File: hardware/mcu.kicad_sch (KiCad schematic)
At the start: 0 parts

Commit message: Add MCU sheet
ESP32-S3-WROOM-1-N8 with 3V3 decoupling, EN RC with reset button,
GPIO0 pull-up with boot button, eject button, status LED, USB series
resistors with DNP filter caps, UART and SPI clock series resistors,
and Tag-Connect TC2030-NL service footprint (excluded from BOM).
Module pin assignment per docs/PCB_DESIGN.md.

Co-Authored-By: Claude Opus 5.5 <noreply@anthropic.com>
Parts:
- added C301: 100uF, Capacitor_SMD:C_1210_3225Metric, symbol Device:C
- added C302: 10uF, Capacitor_SMD:C_0805_2012Metric, symbol Device:C
- added C303: 100nF, Capacitor_SMD:C_0402_1005Metric, symbol Device:C
- added C304: 1uF, Capacitor_SMD:C_0402_1005Metric, symbol Device:C
- added C305, C306, C307, C308: DNP, Capacitor_SMD:C_0402_1005Metric, symbol Device:C
- added D301: Green, LED_SMD:LED_0603_1608Metric, symbol Device:LED
- added J301: TC2030-NL, Connector:Tag-Connect_TC2030-IDC-NL_2x03_P1.27mm_Vertical, symbol Connector_Generic:Conn_02x03_Odd_Even
- added R301, R302: 10k, Resistor_SMD:R_0402_1005Metric, symbol Device:R
- added R303: 1k, Resistor_SMD:R_0402_1005Metric, symbol Device:R
- added R304, R305, R309, R310: 0R, Resistor_SMD:R_0402_1005Metric, symbol Device:R
- added R306: 499R, Resistor_SMD:R_0402_1005Metric, symbol Device:R
- added R307, R308: 100R, Resistor_SMD:R_0402_1005Metric, symbol Device:R
- added SW301: RESET, symbol Switch:SW_Push
- added SW302: BOOT, symbol Switch:SW_Push
- added SW303: EJECT, symbol Switch:SW_Push
- added U301: ESP32-S3-WROOM-1-N8, RF_Module:ESP32-S3-WROOM-1, symbol RF_Module:ESP32-S3-WROOM-1
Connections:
- new net +3V3: C301.1, C302.1, C303.1, J301.1 (Pin_1), R301.1, R302.1, U301.2 (3V3)
- new net BOOT: J301.5 (Pin_5), R302.2, SW302.1, U301.27 (IO0)
- new net EJECT: SW303.1, U301.4 (IO4)
- new net EN: C304.1, J301.3 (Pin_3), R301.2, SW301.1, U301.3 (EN)
- new net GND: C301.2, C302.2, C303.2, C304.2, C305.2, C306.2, C307.2, C308.2, D301.1 (K), J301.6 (Pin_6), SW301.2, SW302.2, SW303.2, U301.1 (GND), U301.40 (GND), U301.41 (GND)
- new net GNSS_PPS: U301.24 (IO47)
- new net GNSS_RESET_N: U301.7 (IO7)
- new net GNSS_RXD: R307.2
- new net GNSS_TXD: R308.2
- new net IO12_SCK: R309.1, U301.20 (IO12)
- new net IO16_SCK: R310.1, U301.9 (IO16)
- new net IO17_TX: R307.1, U301.10 (IO17)
- new net IO18_RX: R308.1, U301.11 (IO18)
- new net IO19_DN: C306.1, R305.2, U301.13 (USB_D-)
- new net IO20_DP: C305.1, R304.2, U301.14 (USB_D+)
- new net LED: R303.1, U301.38 (IO2)
- new net LED_A: D301.2 (A), R303.2
- new net LORA_DIO0: U301.25 (IO48)
- new net LORA_DIO1: U301.35 (IO42)
- new net LORA_MISO: U301.23 (IO21)
- new net LORA_MOSI: U301.8 (IO15)
- new net LORA_NSS: U301.22 (IO14)
- new net LORA_RESET: U301.31 (IO38)
- new net LORA_SCK: C308.1, R310.2
- new net OLED_RES: U301.34 (IO41)
- new net OLED_SCL: U301.17 (IO9)
- new net OLED_SDA: U301.12 (IO8)
- new net SD_CS: U301.18 (IO10)
- new net SD_MISO: U301.21 (IO13)
- new net SD_MOSI: U301.19 (IO11)
- new net SD_SCK: C307.1, R309.2
- new net TXD0_R: R306.1, U301.37 (TXD0)
- new net UART0_RX: J301.4 (Pin_4), U301.36 (RXD0)
- new net UART0_TX: J301.2 (Pin_2), R306.2
- new net USB_DN: R305.1
- new net USB_DP: R304.1
- new net VBUS_SENSE: U301.5 (IO5)
- no-connect marks 0 -> 10

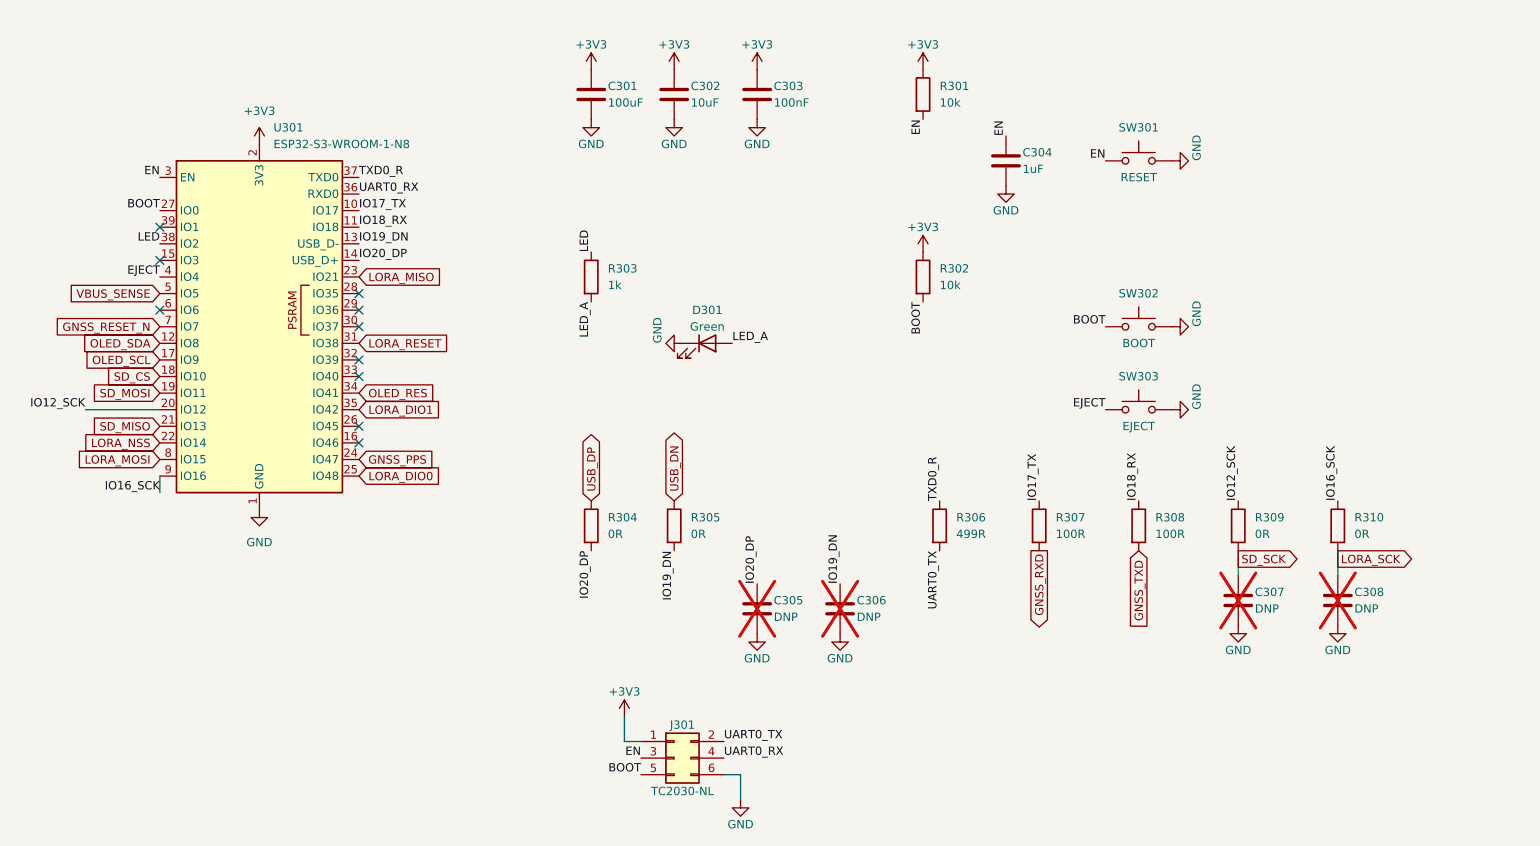
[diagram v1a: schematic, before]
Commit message: Complete schematic, place and partially route the PCB
Schematic:
- Add Storage & Display sheet (microSD, FH12 OLED connector, TLV75801
  3.8 V VBAT regulator, charge-pump parts) and Radio sheet fixes
- Select remaining parts (PTS810, 1206L075THYR, SMF5.0A, MCP120 EN
  supervisor DNP, Elna DSK backup cap), add mounting holes and fiducials
- Pin changes for routability: PPS -> IO15, LoRa MOSI -> IO47,
  LoRa RESET -> IO48, LoRa DIO0 -> IO1
- Remove optional SPI clock filter parts (R309/C307, R310/C308)
- Remove company name from title blocks (personal project)

PCB (60 x 120 mm, 4 layers):
- Place all parts; GNSS zone with custom DRC rules (kicad_dru)
- Project ESP32-S3-WROOM-1 footprint with 0.4 mm thermal vias
- GND / +3V3 / +5V copper zones
- Route power path, GNSS, microSD and LoRa buses
- DRC clean except unrouted nets and expected silkscreen-at-edge items

Docs: selected-parts table, pin table and EMC deviation in PCB_DESIGN.md

Co-Authored-By: Claude Opus 5.5 <noreply@anthropic.com>
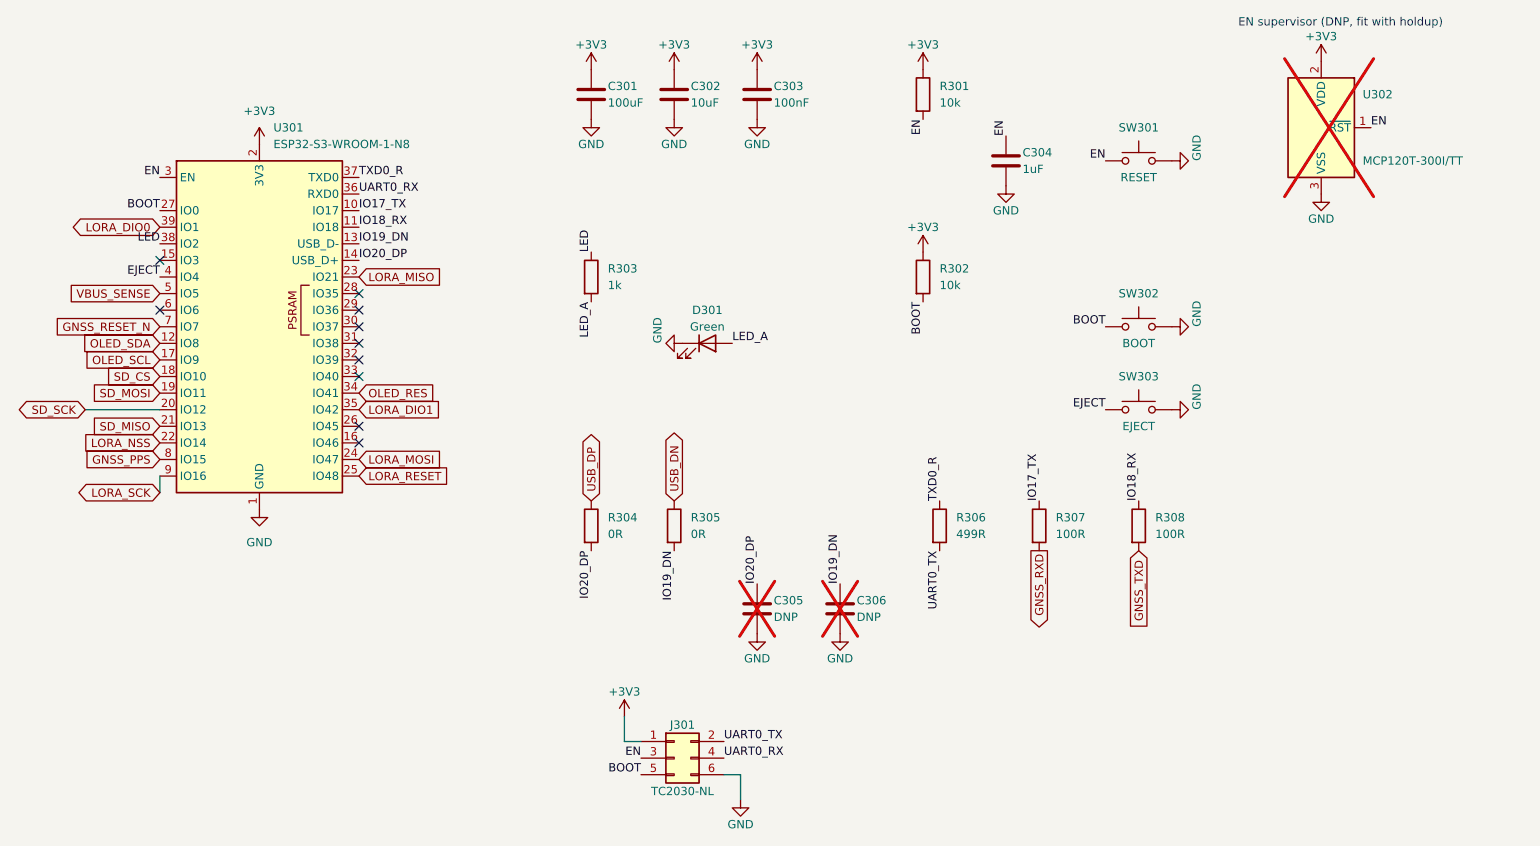
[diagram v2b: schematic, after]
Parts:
- removed C307, C308: DNP, Capacitor_SMD:C_0402_1005Metric, symbol Device:C
- removed R309, R310: 0R, Resistor_SMD:R_0402_1005Metric, symbol Device:R
- added U302: MCP120T-300I/TT, Package_TO_SOT_SMD:SOT-23, symbol Power_Supervisor:MCP120-xxxxTT
- SW301, SW302, SW303: footprint (none) -> Button_Switch_SMD:SW_SPST_PTS810
- U301: footprint RF_Module:ESP32-S3-WROOM-1 -> gps-lora:ESP32-S3-WROOM-1
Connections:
- net IO12_SCK is gone; now on net SD_SCK: U301.20 (IO12)
- net IO16_SCK is gone; now on net LORA_SCK: U301.9 (IO16)
- net +3V3: now also U302.2 (VDD)
- net EN: now also U302.1 (~{RST})
- net GND: now also U302.3 (VSS)
- net GNSS_PPS: now also U301.8 (IO15); no longer U301.24 (IO47)
- net LORA_DIO0: now also U301.39 (IO1); no longer U301.25 (IO48)
- net LORA_MOSI: now also U301.24 (IO47); no longer U301.8 (IO15)
- net LORA_RESET: now also U301.25 (IO48); no longer U301.31 (IO38)
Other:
- note added: "EN supervisor (DNP, fit with holdup)"
- company: SSS-Defence -> (none)

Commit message: Finish PCB routing, add BOM part numbers and fab export
Routing (DRC: 0 errors, 0 unconnected; ERC: 0)
- Complete the remaining nets on top of the GUI routing; GND stitching
  grid and edge fence; every GND pad reaches the L2 plane
- Re-lay the microSD bus under USB D+ so the USBLC6 and VBUS TVS get
  direct GND vias; lift LoRa NSS/MISO/MOSI to clear the TVS via
- Reroute D-, VBUS sense, CC2, BOOT, OLED SDA/SCL, LED and TXD0_R; remove
  vias in pads (R205, R505, R204, R507, U301 pin 7)
- Placement tweaks: C306 moved, C508/C509/R508 rotated 180, R302 moved
- PCB title block with rev v0.1

Parts and outputs
- MPN and Manufacturer fields on all placed parts (tools/add-mpn.py)
- tools/fab-export.py: ERC/DRC gate, zone refill, Gerbers, drill, BOM,
  pick-and-place and fab notes for Lion Circuits
- OLED panel DS501: schematic symbol and board-only 3D footprint
- Elna DSK footprint for C403 (not placed yet)
- kicad-routing skill under .claude/skills

Open before fab (see docs/PCB_DESIGN.md Open items): J502 pin order is
mirrored against the panel FPC; Lion stackup widths; C403 placement.

Co-Authored-By: Claude Opus 5.5 <noreply@anthropic.com>
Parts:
- C301: MPN (none) -> GRM32ER61A107ME20L; Manufacturer (none) -> Murata
- C302: MPN (none) -> CL21A106KAYNNNE; Manufacturer (none) -> Samsung
- C303: MPN (none) -> CL05B104KO5NNNC; Manufacturer (none) -> Samsung
- C304: MPN (none) -> CL05A105KA5NQNC; Manufacturer (none) -> Samsung
- D301: MPN (none) -> LTST-C191KGKT; Manufacturer (none) -> Lite-On
- R301, R302: MPN (none) -> RC0402FR-0710KL; Manufacturer (none) -> Yageo
- R303: MPN (none) -> RC0402FR-071KL; Manufacturer (none) -> Yageo
- R304, R305: MPN (none) -> RC0402JR-070RL; Manufacturer (none) -> Yageo
- R306: MPN (none) -> RC0402FR-07499RL; Manufacturer (none) -> Yageo
- R307, R308: MPN (none) -> RC0402FR-07100RL; Manufacturer (none) -> Yageo
- SW301, SW302, SW303: MPN (none) -> PTS810 SJM 250 SMTR LFS; Manufacturer (none) -> C&K
- U301: MPN (none) -> ESP32-S3-WROOM-1-N8; Manufacturer (none) -> Espressif
- U302: MPN (none) -> MCP120T-300I/TT; Manufacturer (none) -> Microchip

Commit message: Rename project to Theoros and add V1.0 silkscreen artwork
Theoros (Greek θεωρός): an official observer and envoy, sent to watch
and report back.

Rename gps-lora to theoros everywhere: KiCad project, symbol and
footprint libraries, firmware library (theoros-core), umbrella header,
PC tool (tools/theoros.py), NVS namespaces, mDNS hostname, docs and
title blocks. The HKDF salt is now "theoros" (7 bytes), so every derived
key changes; the SECURITY.md test vectors are recomputed and host tests
pass. Boards provisioned with the old salt need re-provisioning.

Board revision is now V1.0. Silkscreen additions:
- Top: "THEOROS ${REVISION}" and "ΘΕΩΡΟΣ", an antenna warning next to
  J401, and a hidden line under the OLED panel.
- Bottom: an owl made as a solder-mask opening over the GND pour (gold
  with ENIG; vias inside stay tented) and the motto "ΟΡΩ ΚΑΙ ΑΓΓΕΛΛΩ /
  I SEE AND I REPORT".
Fab notes now state silkscreen on both sides and the intentional mask
opening. DRC is unchanged from before (4 silk-edge warnings).

Co-Authored-By: Claude Opus 5.5 <noreply@anthropic.com>
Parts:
- U301: footprint gps-lora:ESP32-S3-WROOM-1 -> theoros:ESP32-S3-WROOM-1
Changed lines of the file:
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@@
 		(title "MCU")
 		(date "2026-10-05")
-		(rev "v0.1")
+		(rev "V1.0")
 		(comment 1 "CERN-OHL-P-2.0")
-		(comment 2 "https://github.com/Majorwhiskey/gps-lora")
+		(comment 2 "https://github.com/Majorwhiskey/theoros")
 	)
 	(text "EN supervisor (DNP, fit with holdup)"
@@
 		)
 		(instances
-			(project "gps-lora"
+			(project "theoros"
 				(path "/4fe56230-194d-489d-a2bc-70162e8e6b48/4a1b2dd0-e07f-4468-b434-479773685126"
 					(reference "SW303")
@@
 		)
 		(instances
-			(project "gps-lora"
+			(project "theoros"
 				(path "/4fe56230-194d-489d-a2bc-70162e8e6b48/4a1b2dd0-e07f-4468-b434-479773685126"
 					(reference "R305")
@@
 		)
 		(instances
-			(project "gps-lora"
+			(project "theoros"
 				(path "/4fe56230-194d-489d-a2bc-70162e8e6b48/4a1b2dd0-e07f-4468-b434-479773685126"
 					(reference "SW301")
@@
 		)
 		(instances
-			(project "gps-lora"
+			(project "theoros"
 				(path "/4fe56230-194d-489d-a2bc-70162e8e6b48/4a1b2dd0-e07f-4468-b434-479773685126"
 					(reference "#PWR41")
@@
 		)
 		(instances
-			(project "gps-lora"
+			(project "theoros"
 				(path "/4fe56230-194d-489d-a2bc-70162e8e6b48/4a1b2dd0-e07f-4468-b434-479773685126"
 					(reference "C305")
@@
 		)
 		(instances
-			(project "gps-lora"
+			(project "theoros"
 				(path "/4fe56230-194d-489d-a2bc-70162e8e6b48/4a1b2dd0-e07f-4468-b434-479773685126"
 					(reference "#PWR35")
@@
 		)
 		(instances
-			(project "gps-lora"
+			(project "theoros"
 				(path "/4fe56230-194d-489d-a2bc-70162e8e6b48/4a1b2dd0-e07f-4468-b434-479773685126"
 					(reference "#PWR32")
@@
 		)
 		(instances
-			(project "gps-lora"
+			(project "theoros"
 				(path "/4fe56230-194d-489d-a2bc-70162e8e6b48/4a1b2dd0-e07f-4468-b434-479773685126"
 					(reference "C301")
@@
 		)
 		(instances
-			(project "gps-lora"
+			(project "theoros"
 				(path "/4fe56230-194d-489d-a2bc-70162e8e6b48/4a1b2dd0-e07f-4468-b434-479773685126"
 					(reference "R303")
@@
 			)
 		)
-		(property "Footprint" "gps-lora:ESP32-S3-WROOM-1"
+		(property "Footprint" "theoros:ESP32-S3-WROOM-1"
 			(at 88.9 114.3 0)
 			(hide yes)
@@
 		)
 		(instances
-			(project "gps-lora"
+			(project "theoros"
 				(path "/4fe56230-194d-489d-a2bc-70162e8e6b48/4a1b2dd0-e07f-4468-b434-479773685126"
 					(reference "#PWR028")
@@
 		)
 		(instances
-			(project "gps-lora"
+			(project "theoros"
 				(path "/4fe56230-194d-489d-a2bc-70162e8e6b48/4a1b2dd0-e07f-4468-b434-479773685126"
 					(reference "#PWR36")
@@
 		)
 		(instances
-			(project "gps-lora"
+			(project "theoros"
 				(path "/4fe56230-194d-489d-a2bc-70162e8e6b48/4a1b2dd0-e07f-4468-b434-479773685126"
 					(reference "#PWR39")
@@
 		)
 		(instances
-			(project "gps-lora"
+			(project "theoros"
 				(path "/4fe56230-194d-489d-a2bc-70162e8e6b48/4a1b2dd0-e07f-4468-b434-479773685126"
 					(reference "#PWR601")
@@
 		)
 		(instances
-			(project "gps-lora"
+			(project "theoros"
 				(path "/4fe56230-194d-489d-a2bc-70162e8e6b48/4a1b2dd0-e07f-4468-b434-479773685126"
 					(reference "SW302")
@@
 		)
 		(instances
-			(project "gps-lora"
+			(project "theoros"
 				(path "/4fe56230-194d-489d-a2bc-70162e8e6b48/4a1b2dd0-e07f-4468-b434-479773685126"
 					(reference "#PWR602")
@@
 			)
 		)
-		(property "Footprint" "gps-lora:ESP32-S3-WROOM-1"
+		(property "Footprint" "theoros:ESP32-S3-WROOM-1"
 			(at 88.9 83.82 0)
 			(hide yes)
@@
 		)
 		(instances
-			(project "gps-lora"
+			(project "theoros"
 				(path "/4fe56230-194d-489d-a2bc-70162e8e6b48/4a1b2dd0-e07f-4468-b434-479773685126"
 					(reference "U301")
@@
 		)
 		(instances
-			(project "gps-lora"
+			(project "theoros"
 				(path "/4fe56230-194d-489d-a2bc-70162e8e6b48/4a1b2dd0-e07f-4468-b434-479773685126"
 					(reference "#PWR50")
@@
 		)
 		(instances
-			(project "gps-lora"
+			(project "theoros"
 				(path "/4fe56230-194d-489d-a2bc-70162e8e6b48/4a1b2dd0-e07f-4468-b434-479773685126"
 					(reference "#PWR33")
@@
 		)
 		(instances
-			(project "gps-lora"
+			(project "theoros"
 				(path "/4fe56230-194d-489d-a2bc-70162e8e6b48/4a1b2dd0-e07f-4468-b434-479773685126"
 					(reference "R308")
@@
 		)
 		(instances
-			(project "gps-lora"
+			(project "theoros"
 				(path "/4fe56230-194d-489d-a2bc-70162e8e6b48/4a1b2dd0-e07f-4468-b434-479773685126"
 					(reference "C303")
@@
 		)
 		(instances
-			(project "gps-lora"
+			(project "theoros"
 				(path "/4fe56230-194d-489d-a2bc-70162e8e6b48/4a1b2dd0-e07f-4468-b434-479773685126"
 					(reference "#PWR38")
@@
 		)
 		(instances
-			(project "gps-lora"
+			(project "theoros"
 				(path "/4fe56230-194d-489d-a2bc-70162e8e6b48/4a1b2dd0-e07f-4468-b434-479773685126"
 					(reference "U302")
@@
 		)
 		(instances
-			(project "gps-lora"
+			(project "theoros"
 				(path "/4fe56230-194d-489d-a2bc-70162e8e6b48/4a1b2dd0-e07f-4468-b434-479773685126"
 					(reference "R304")
@@
 		)
 		(instances
-			(project "gps-lora"
+			(project "theoros"
 				(path "/4fe56230-194d-489d-a2bc-70162e8e6b48/4a1b2dd0-e07f-4468-b434-479773685126"
 					(reference "R301")
@@
 		)
 		(instances
-			(project "gps-lora"
+			(project "theoros"
 				(path "/4fe56230-194d-489d-a2bc-70162e8e6b48/4a1b2dd0-e07f-4468-b434-479773685126"
 					(reference "#PWR37")
@@
 		)
 		(instances
-			(project "gps-lora"
+			(project "theoros"
 				(path "/4fe56230-194d-489d-a2bc-70162e8e6b48/4a1b2dd0-e07f-4468-b434-479773685126"
 					(reference "#PWR45")
@@
 		)
 		(instances
-			(project "gps-lora"
+			(project "theoros"
 				(path "/4fe56230-194d-489d-a2bc-70162e8e6b48/4a1b2dd0-e07f-4468-b434-479773685126"
 					(reference "J301")
@@
 		)
 		(instances
-			(project "gps-lora"
+			(project "theoros"
 				(path "/4fe56230-194d-489d-a2bc-70162e8e6b48/4a1b2dd0-e07f-4468-b434-479773685126"
 					(reference "#PWR51")
@@
 		)
 		(instances
-			(project "gps-lora"
+			(project "theoros"
 				(path "/4fe56230-194d-489d-a2bc-70162e8e6b48/4a1b2dd0-e07f-4468-b434-479773685126"
 					(reference "#PWR31")
@@
 		)
 		(instances
-			(project "gps-lora"
+			(project "theoros"
 				(path "/4fe56230-194d-489d-a2bc-70162e8e6b48/4a1b2dd0-e07f-4468-b434-479773685126"
 					(reference "R307")
@@
 		)
 		(instances
-			(project "gps-lora"
+			(project "theoros"
 				(path "/4fe56230-194d-489d-a2bc-70162e8e6b48/4a1b2dd0-e07f-4468-b434-479773685126"
 					(reference "R306")
@@
 		)
 		(instances
-			(project "gps-lora"
+			(project "theoros"
 				(path "/4fe56230-194d-489d-a2bc-70162e8e6b48/4a1b2dd0-e07f-4468-b434-479773685126"
 					(reference "#PWR40")
@@
 		)
 		(instances
-			(project "gps-lora"
+			(project "theoros"
 				(path "/4fe56230-194d-489d-a2bc-70162e8e6b48/4a1b2dd0-e07f-4468-b434-479773685126"
 					(reference "#PWR34")
@@
 		)
 		(instances
-			(project "gps-lora"
+			(project "theoros"
 				(path "/4fe56230-194d-489d-a2bc-70162e8e6b48/4a1b2dd0-e07f-4468-b434-479773685126"
 					(reference "#PWR42")
@@
 		)
 		(instances
-			(project "gps-lora"
+			(project "theoros"
 				(path "/4fe56230-194d-489d-a2bc-70162e8e6b48/4a1b2dd0-e07f-4468-b434-479773685126"
 					(reference "C306")
@@
 		)
 		(instances
-			(project "gps-lora"
+			(project "theoros"
 				(path "/4fe56230-194d-489d-a2bc-70162e8e6b48/4a1b2dd0-e07f-4468-b434-479773685126"
 					(reference "R302")
@@
 		)
 		(instances
-			(project "gps-lora"
+			(project "theoros"
 				(path "/4fe56230-194d-489d-a2bc-70162e8e6b48/4a1b2dd0-e07f-4468-b434-479773685126"
 					(reference "C304")
@@
 		)
 		(instances
-			(project "gps-lora"
+			(project "theoros"
 				(path "/4fe56230-194d-489d-a2bc-70162e8e6b48/4a1b2dd0-e07f-4468-b434-479773685126"
 					(reference "#PWR43")
@@
 		)
 		(instances
-			(project "gps-lora"
+			(project "theoros"
 				(path "/4fe56230-194d-489d-a2bc-70162e8e6b48/4a1b2dd0-e07f-4468-b434-479773685126"
 					(reference "#PWR44")
@@
 		)
 		(instances
-			(project "gps-lora"
+			(project "theoros"
 				(path "/4fe56230-194d-489d-a2bc-70162e8e6b48/4a1b2dd0-e07f-4468-b434-479773685126"
 					(reference "C302")
@@
 		)
 		(instances
-			(project "gps-lora"
+			(project "theoros"
 				(path "/4fe56230-194d-489d-a2bc-70162e8e6b48/4a1b2dd0-e07f-4468-b434-479773685126"
 					(reference "#PWR029")
@@
 		)
 		(instances
-			(project "gps-lora"
+			(project "theoros"
 				(path "/4fe56230-194d-489d-a2bc-70162e8e6b48/4a1b2dd0-e07f-4468-b434-479773685126"
 					(reference "D301")
